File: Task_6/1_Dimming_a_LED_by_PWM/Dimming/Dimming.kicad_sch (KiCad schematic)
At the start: 5 parts, among them Q1 IC=0.5 VCEO=45

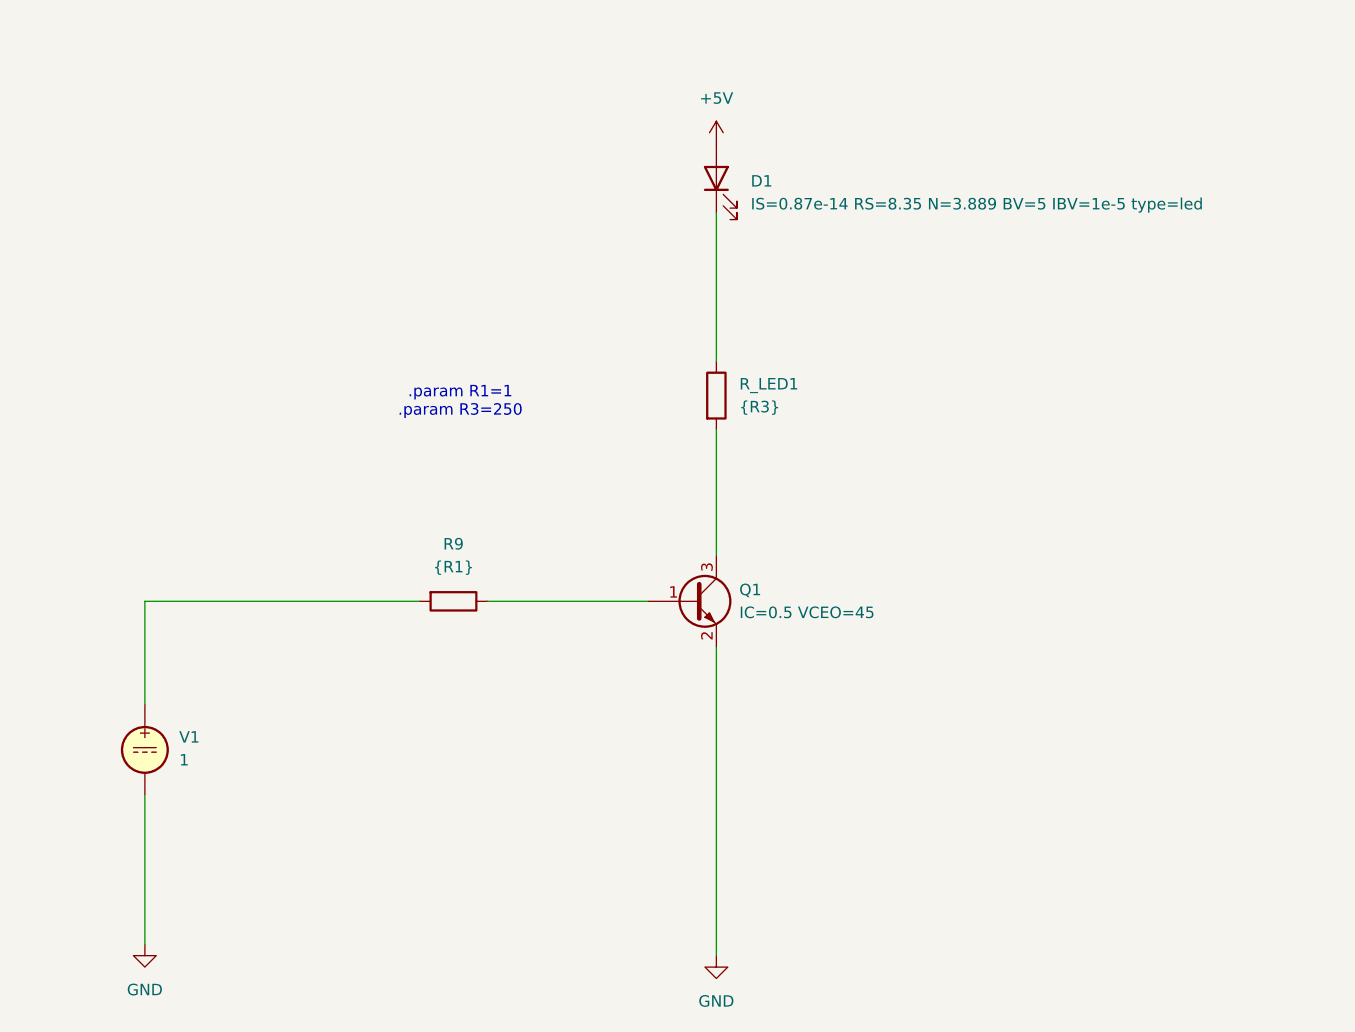
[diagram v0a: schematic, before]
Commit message: Added model to LED, Transistor and VSOURCE
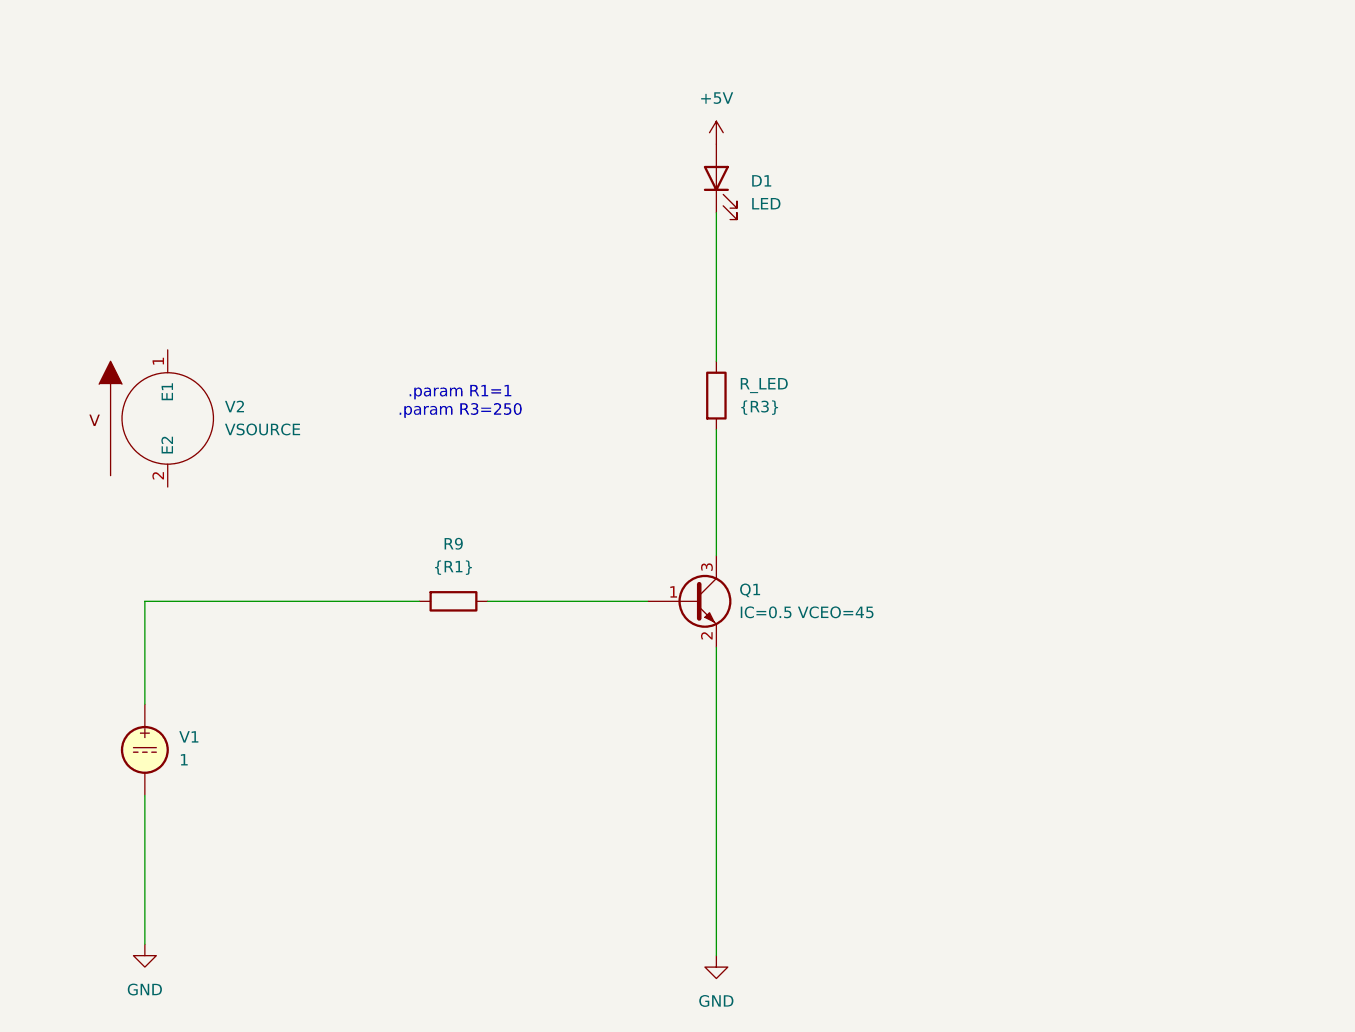
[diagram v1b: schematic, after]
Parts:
- added V2: VSOURCE, symbol pspice:VSOURCE
- D1: value IS=0.87e-14 RS=8.35 N=3.889 BV=5 IBV=1e-5 type=led -> LED
- renumbered R_LED1 to R_LED
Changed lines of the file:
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@@
+	)
+	(symbol
+		(lib_id "pspice:VSOURCE")
+		(at 97.79 71.12 0)
+		(unit 1)
+		(exclude_from_sim no)
+		(in_bom yes)
+		(on_board yes)
+		(dnp no)
+		(fields_autoplaced yes)
+		(property "Reference" "V2"
+			(at 104.14 69.8499 0)
+			(effects
+				(font
+					(size 1.27 1.27)
+				)
+				(justify left)
+			)
+		)
+		(property "Value" "VSOURCE"
+			(at 104.14 72.3899 0)
+			(effects
+				(font
+					(size 1.27 1.27)
+				)
+				(justify left)
+			)
+		)
+		(property "Footprint" ""
+			(at 97.79 71.12 0)
+			(effects
+				(font
+					(size 1.27 1.27)
+				)
+				(hide yes)
+			)
+		)
+		(property "Datasheet" ""
+			(at 97.79 71.12 0)
+			(effects
+				(font
+					(size 1.27 1.27)
+				)
+				(hide yes)
+			)
+		)
+		(property "Description" ""
+			(at 97.79 71.12 0)
+			(effects
+				(font
+					(size 1.27 1.27)
+				)
+				(hide yes)
+			)
+		)
+		(pin "1"
+		)
+		(pin "2"
+		)
+		(instances
+			(project ""
+				(path "/0cfaf9bc-a933-40bc-9237-d4ec7dcd84ea"
+					(reference "V2")
+					(unit 1)
+				)
+			)
+		)
 	)
 	(symbol
@@
 			)
 		)
+		(property "Sim.Library" "BC817-25.kicad_mod"
+			(at 156.21 91.44 0)
+			(effects
+				(font
+					(size 1.27 1.27)
+				)
+				(hide yes)
+			)
+		)
+		(property "Sim.Name" "BC817_25"
+			(at 156.21 91.44 0)
+			(effects
+				(font
+					(size 1.27 1.27)
+				)
+				(hide yes)
+			)
+		)
+		(property "Sim.Device" "SUBCKT"
+			(at 156.21 91.44 0)
+			(effects
+				(font
+					(size 1.27 1.27)
+				)
+				(hide yes)
+			)
+		)
+		(property "Sim.Pins" "1=1 2=2 3=3"
+			(at 156.21 91.44 0)
+			(effects
+				(font
+					(size 1.27 1.27)
+				)
+				(hide yes)
+			)
+		)
 		(pin "1"
 		)
@@
 			)
 		)
-		(property "Value" "IS=0.87e-14 RS=8.35 N=3.889 BV=5 IBV=1e-5 type=led"
+		(property "Value" "LED"
 			(at 162.56 47.3074 90)
 			(effects
@@
 		)
 		(property "Description" "Light emitting diode"
+			(at 158.75 44.45 0)
+			(effects
+				(font
+					(size 1.27 1.27)
+				)
+				(hide yes)
+			)
+		)
+		(property "Sim.Library" "SLX-LX5093UWC.kicad_mod"
+			(at 158.75 44.45 0)
+			(effects
+				(font
+					(size 1.27 1.27)
+				)
+				(hide yes)
+			)
+		)
+		(property "Sim.Name" "SLX-LX5093UWC"
+			(at 158.75 44.45 0)
+			(effects
+				(font
+					(size 1.27 1.27)
+				)
+				(hide yes)
+			)
+		)
+		(property "Sim.Device" "D"
+			(at 158.75 44.45 0)
+			(effects
+				(font
+					(size 1.27 1.27)
+				)
+				(hide yes)
+			)
+		)
+		(property "Sim.Pins" "1=A 2=K"
 			(at 158.75 44.45 0)
 			(effects
@@
 		(dnp no)
 		(fields_autoplaced yes)
-		(property "Reference" "R_LED1"
+		(property "Reference" "R_LED"
 			(at 161.29 67.3099 0)
 			(effects
@@
 			(project ""
 				(path "/0cfaf9bc-a933-40bc-9237-d4ec7dcd84ea"
-					(reference "R_LED1")
-					(unit 1)
-				)
+					(reference "R_LED")
+					(unit 1)
+				)

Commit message: Expanded 6
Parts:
- removed R9: {R1}, symbol Device:R
- removed R_LED: {R3}, symbol Device:R
- removed V1: 1, symbol Simulation_SPICE:VDC
- removed V2: VSOURCE, symbol pspice:VSOURCE
- added R1: 1, symbol Device:R
- added R2: 250, symbol Device:R
- added V1, V2: VSIN, symbol Simulation_SPICE:VSIN
- Q1: value IC=0.5 VCEO=45 -> BC817
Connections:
- net GND: now also V1.2, V2.2
- net output: now reaches Q1.1 (B)
- net output: now also R1.1
- net at Q1.3 (C): now also R2.2
- net +5V: no longer names the net of D1.2 (A)
- new net full: R2.1, V2.1
- new net source: R1.2, V1.1
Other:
- note removed: ".param R1=1 .param R3=250"

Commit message: Work on 6)
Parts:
- removed V2: VSIN, symbol Simulation_SPICE:VSIN
- added V2: 5, symbol Simulation_SPICE:VDC
- R2: value 250 -> 300
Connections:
- net GND: now also V2.2
- net full: now also V2.1
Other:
- moved on the sheet: D1, R1, R2

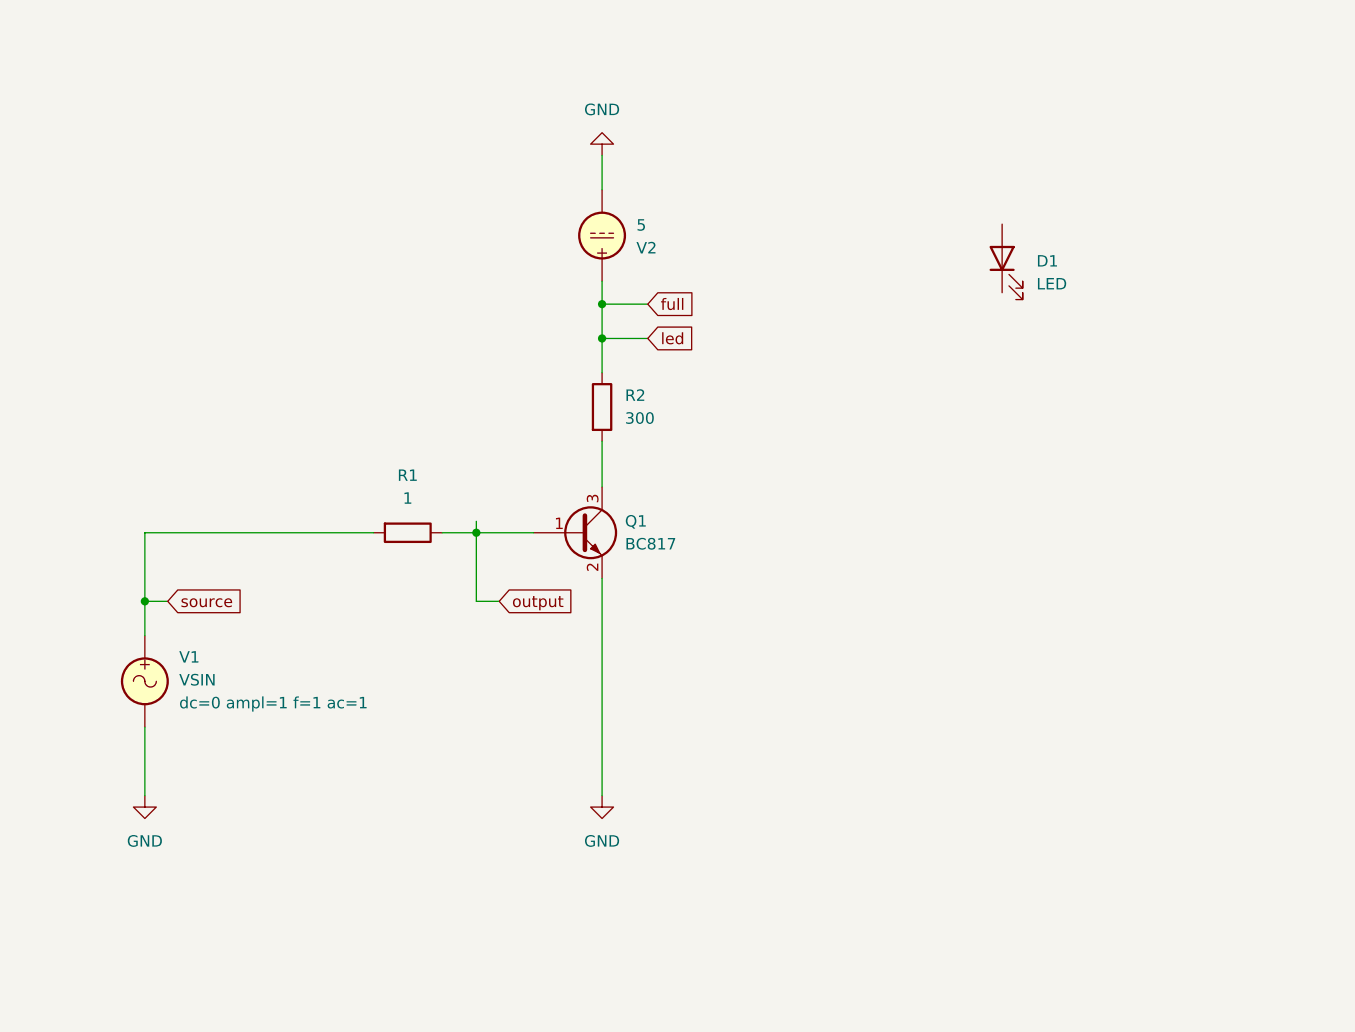
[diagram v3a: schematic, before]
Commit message: Fixed 6 KiCAD
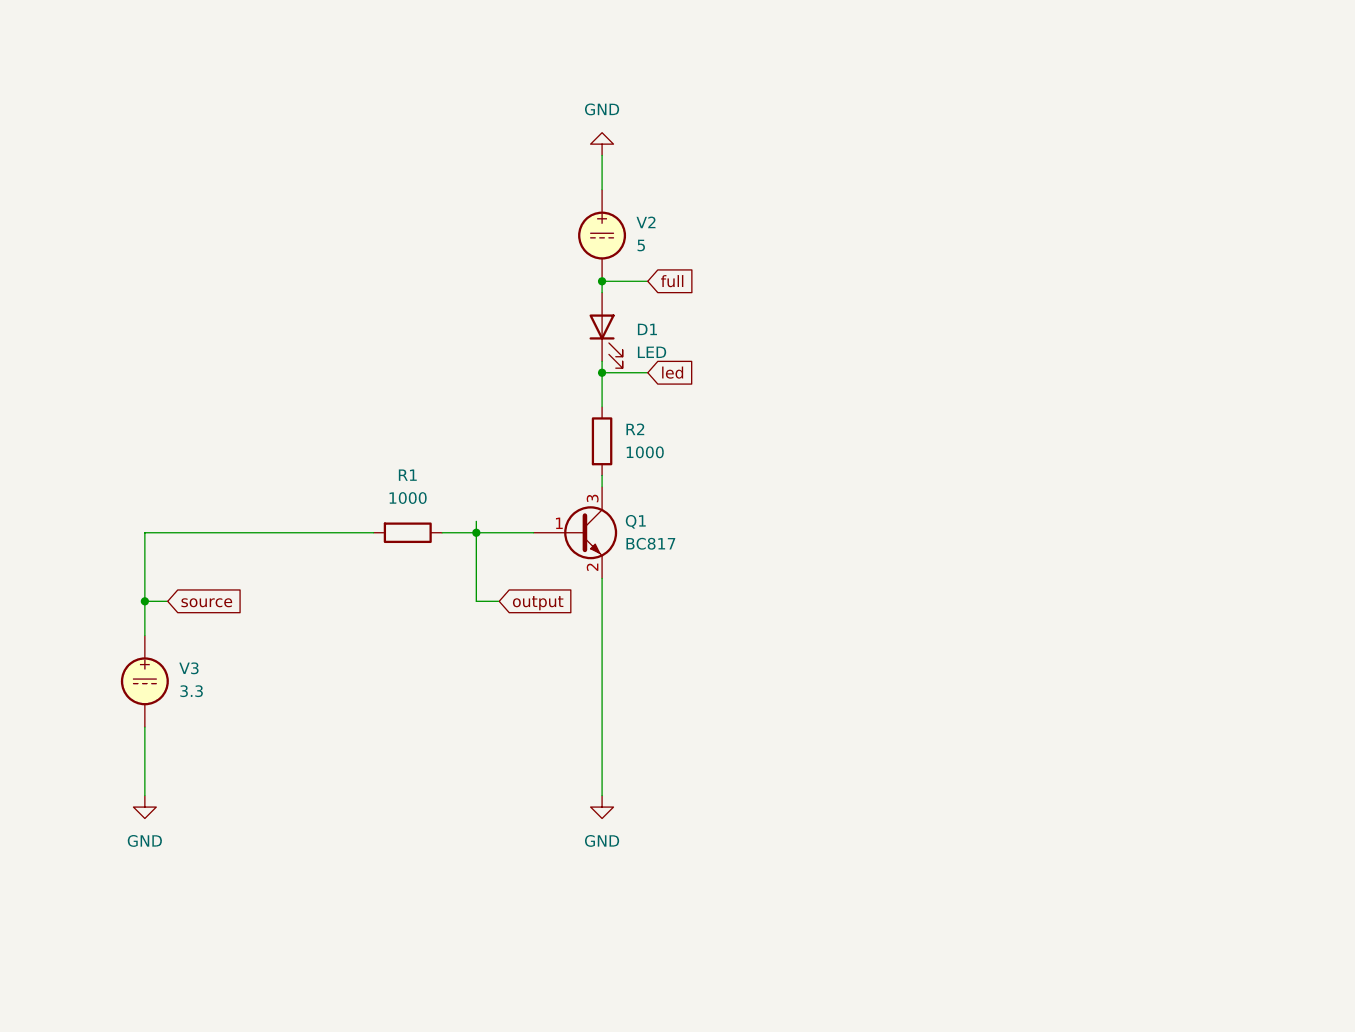
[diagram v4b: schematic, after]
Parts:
- removed V1: VSIN, symbol Simulation_SPICE:VSIN
- added V3: 3.3, symbol Simulation_SPICE:VDC
- R1: value 1 -> 1000
- R2: value 300 -> 1000
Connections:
- net GND: now also V2.1, V3.2; no longer V2.2
- net full: now also D1.2 (A), V2.2; no longer R2.1, V2.1
- net source: now also V3.1
- net led: now reaches D1.1 (K)
- net led: now also R2.1
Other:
- moved on the sheet: D1, R2
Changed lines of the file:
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@@
 	(paper "A4")
-	(junction
-		(at 146.05 58.42)
-		(diameter 0)
-		(color 0 0 0 0)
-	)
 	(junction
 		(at 132.08 83.82)
@@
 	)
 	(junction
-		(at 146.05 62.23)
+		(at 146.05 55.88)
 		(diameter 0)
 		(color 0 0 0 0)
 	)
+	(junction
+		(at 146.05 66.04)
+		(diameter 0)
+		(color 0 0 0 0)
+	)
 	(wire
 		(pts
@@
 	(wire
 		(pts
-			(xy 146.05 73.66) (xy 146.05 78.74)
+			(xy 146.05 77.47) (xy 146.05 78.74)
 		)
 		(stroke
@@
 	(wire
 		(pts
+			(xy 146.05 69.85) (xy 146.05 66.04)
+		)
+		(stroke
+			(width 0)
+			(type default)
+		)
+	)
+	(wire
+		(pts
 			(xy 146.05 88.9) (xy 146.05 113.03)
 		)
@@
 	(wire
 		(pts
-			(xy 151.13 58.42) (xy 146.05 58.42)
-		)
-		(stroke
-			(width 0)
-			(type default)
-		)
-	)
-	(wire
-		(pts
-			(xy 146.05 55.88) (xy 146.05 58.42)
-		)
-		(stroke
-			(width 0)
-			(type default)
-		)
-	)
-	(wire
-		(pts
-			(xy 146.05 62.23) (xy 146.05 66.04)
+			(xy 146.05 55.88) (xy 146.05 57.15)
+		)
+		(stroke
+			(width 0)
+			(type default)
+		)
+	)
+	(wire
+		(pts
+			(xy 151.13 55.88) (xy 146.05 55.88)
 		)
 		(stroke
@@
 	(wire
 		(pts
-			(xy 151.13 62.23) (xy 146.05 62.23)
+			(xy 151.13 66.04) (xy 146.05 66.04)
 		)
 		(stroke
@@
 	(wire
 		(pts
+			(xy 146.05 64.77) (xy 146.05 66.04)
+		)
+		(stroke
+			(width 0)
+			(type default)
+		)
+	)
+	(wire
+		(pts
 			(xy 132.08 82.55) (xy 132.08 83.82)
 		)
@@
 		(pts
 			(xy 120.65 83.82) (xy 95.25 83.82)
-		)
-		(stroke
-			(width 0)
-			(type default)
-		)
-	)
-	(wire
-		(pts
-			(xy 146.05 58.42) (xy 146.05 62.23)
 		)
 		(stroke
@@
 	(global_label "full"
 		(shape input)
-		(at 151.13 58.42 0)
+		(at 151.13 55.88 0)
 		(fields_autoplaced yes)
 		(effects
@@
 		)
 		(property "Intersheetrefs" "${INTERSHEET_REFS}"
-			(at 157.3203 58.42 0)
+			(at 157.3203 55.88 0)
 			(effects
 				(font
@@
 	(global_label "led"
 		(shape input)
-		(at 151.13 62.23 0)
+		(at 151.13 66.04 0)
 		(fields_autoplaced yes)
 		(effects
@@
 		)
 		(property "Intersheetrefs" "${INTERSHEET_REFS}"
-			(at 157.018 62.23 0)
+			(at 157.018 66.04 0)
 			(effects
 				(font
@@
 			)
 		)
-		(property "Value" "1"
+		(property "Value" "1000"
 			(at 124.46 80.01 90)
 			(effects
@@
 	(symbol
 		(lib_id "Device:LED")
-		(at 190.5 53.34 90)
+		(at 146.05 60.96 90)
 		(unit 1)
 		(exclude_from_sim no)
@@
 		(on_board yes)
 		(dnp no)
-		(fields_autoplaced yes)
 		(property "Reference" "D1"
-			(at 194.31 53.6574 90)
+			(at 149.86 61.2774 90)
 			(effects
 				(font
@@
 		)
 		(property "Value" "LED"
-			(at 194.31 56.1974 90)
+			(at 149.86 63.8174 90)
 			(effects
 				(font
@@
 		)
 		(property "Footprint" ""
-			(at 190.5 53.34 0)
+			(at 146.05 60.96 0)
 			(effects
 				(font
@@
 		)
 		(property "Datasheet" "~"
-			(at 190.5 53.34 0)
+			(at 146.05 60.96 0)
 			(effects
 				(font
@@
 		)
 		(property "Description" "Light emitting diode"
-			(at 190.5 53.34 0)
+			(at 146.05 60.96 0)
 			(effects
 				(font
@@
 		)
 		(property "Sim.Library" "SLX-LX5093UWC.kicad_mod"
-			(at 190.5 53.34 0)
+			(at 146.05 60.96 0)
 			(effects
 				(font
@@
 		)
 		(property "Sim.Name" "SLX-LX5093UWC"
-			(at 190.5 53.34 0)
+			(at 146.05 60.96 0)
 			(effects
 				(font
@@
 		)
 		(property "Sim.Device" "D"
-			(at 190.5 53.34 0)
+			(at 146.05 60.96 0)
 			(effects
 				(font
@@
 		)
 		(property "Sim.Pins" "1=A 2=K"
-			(at 190.5 53.34 0)
+			(at 146.05 60.96 0)
 			(effects
 				(font
@@
 	(symbol
 		(lib_id "Device:R")
-		(at 146.05 69.85 0)
+		(at 146.05 73.66 0)
 		(unit 1)
 		(exclude_from_sim no)
@@
 		(fields_autoplaced yes)
 		(property "Reference" "R2"
-			(at 148.59 68.5799 0)
-			(effects
-				(font
-					(size 1.27 1.27)
-				)
-				(justify left)
-			)
-		)
-		(property "Value" "300"
-			(at 148.59 71.1199 0)
+			(at 148.59 72.3899 0)
+			(effects
+				(font
+					(size 1.27 1.27)
+				)
+				(justify left)
+			)
+		)
+		(property "Value" "1000"
+			(at 148.59 74.9299 0)
 			(effects
 				(font
@@
 		)
 		(property "Footprint" ""
-			(at 144.272 69.85 90)
+			(at 144.272 73.66 90)
 			(effects
 				(font
@@
 		)
 		(property "Datasheet" "~"
-			(at 146.05 69.85 0)
+			(at 146.05 73.66 0)
 			(effects
 				(font
@@
 		)
 		(property "Description" "Resistor"
-			(at 146.05 69.85 0)
+			(at 146.05 73.66 0)
 			(effects
 				(font
@@
 		(lib_id "Simulation_SPICE:VDC")
 		(at 146.05 50.8 0)
-		(mirror x)
 		(unit 1)
 		(exclude_from_sim no)
@@
 		(dnp no)
 		(property "Reference" "V2"
-			(at 149.86 52.1999 0)
+			(at 149.86 49.4001 0)
 			(effects
 				(font
@@
 		)
 		(property "Value" "5"
-			(at 149.86 49.6599 0)
+			(at 149.86 51.9401 0)
 			(effects
 				(font
@@
 	)
 	(symbol
-		(lib_id "Simulation_SPICE:VSIN")
+		(lib_id "Simulation_SPICE:VDC")
 		(at 95.25 100.33 0)
 		(unit 1)
@@
 		(on_board yes)
 		(dnp no)
-		(property "Reference" "V1"
-			(at 99.06 97.6601 0)
-			(effects
-				(font
-					(size 1.27 1.27)
-				)
-				(justify left)
-			)
-		)
-		(property "Value" "VSIN"
-			(at 99.06 100.2001 0)
+		(fields_autoplaced yes)
+		(property "Reference" "V3"
+			(at 99.06 98.9301 0)
+			(effects
+				(font
+					(size 1.27 1.27)
+				)
+				(justify left)
+			)
+		)
+		(property "Value" "3.3"
+			(at 99.06 101.4701 0)
 			(effects
 				(font
@@
 			)
 		)
-		(property "Description" "Voltage source, sinusoidal"
+		(property "Description" "Voltage source, DC"
 			(at 95.25 100.33 0)
 			(effects
@@
 			)
 		)
-		(property "Sim.Params" "dc=0 ampl=1 f=1 ac=1"
-			(at 99.06 102.7401 0)
-			(effects
-				(font
-					(size 1.27 1.27)
-				)
-				(justify left)
-			)
-		)
-		(property "Sim.Type" "SIN"
+		(property "Sim.Type" "DC"
 			(at 95.25 100.33 0)
 			(effects
@@
 			)
 		)
+		(pin "2"
+		)
 		(pin "1"
-		)
-		(pin "2"
 		)
 		(instances
 			(project ""
 				(path "/b0c10853-3f7b-40c1-b1d0-8a6433951273"
-					(reference "V1")
+					(reference "V3")
 					(unit 1)
 				)
@@
 		(on_board yes)
 		(dnp no)
-		(fields_autoplaced yes)
 		(property "Reference" "Q1"
 			(at 148.59 82.5499 0)

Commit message: Completed 6) Simulation and Measurement
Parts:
- removed V3: 3.3, symbol Simulation_SPICE:VDC
- added V3: VPULSE, symbol Simulation_SPICE:VPULSE
- R2: value 1000 -> 5
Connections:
- net GND: now also V2.2, V3.1; no longer V2.1
- net full: now also V2.1; no longer V2.2
- net source: now also V3.2
- net Resistor: now reaches Q1.3 (C), R2.2
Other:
- moved on the sheet: R1, R2
